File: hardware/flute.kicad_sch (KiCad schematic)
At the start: 17 parts, among them J1 Conn_01x02, J2 AudioJack2, SW1 C, SW2 D, SW3 E, SW4 F, SW5 G, SW6 A, SW7 H, SW8 OCTAVE?

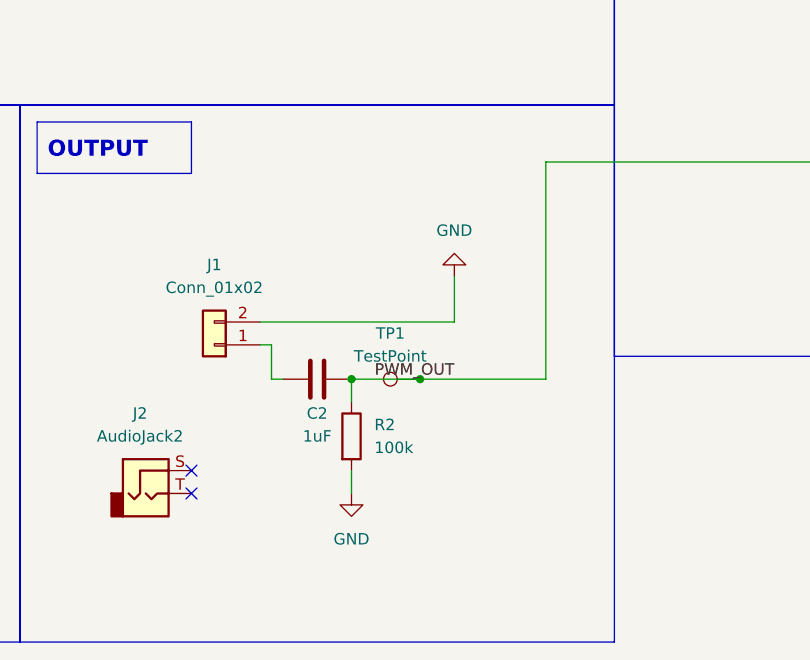
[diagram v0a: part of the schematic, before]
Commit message: output coupling solder jumpers for schematic
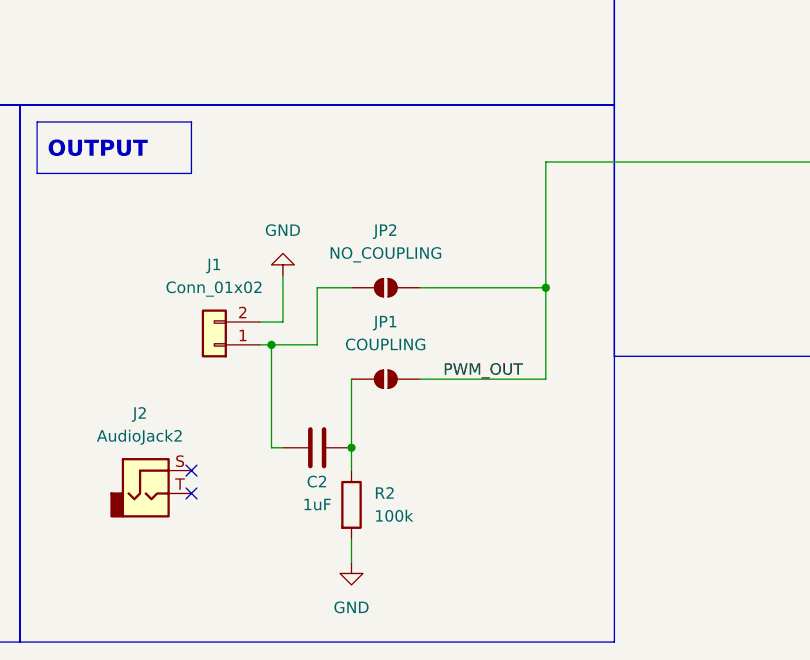
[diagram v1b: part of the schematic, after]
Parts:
- removed TP1: TestPoint, TestPoint:TestPoint_Bridge_Pitch2.54mm_Drill1.3mm, symbol Connector:TestPoint
- added JP1: COUPLING, Jumper:SolderJumper-2_P1.3mm_Open_Pad1.0x1.5mm, symbol Jumper:SolderJumper_2_Open
- added JP2: NO_COUPLING, Jumper:SolderJumper-2_P1.3mm_Open_Pad1.0x1.5mm, symbol Jumper:SolderJumper_2_Open
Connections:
- net PWM_OUT: now also JP1.2 (B), JP2.2 (B); no longer C2.2, R2.1
- net at C2.1, J1.1 (Pin_1): now also JP2.1 (A)
- new net: C2.2, JP1.1 (A), R2.1
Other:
- moved on the sheet: C2, R2
